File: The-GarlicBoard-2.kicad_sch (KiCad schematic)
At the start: 314 parts, among them J1 TYPE-C-31-M12_13, J2 PAD_SQUARE_1MM, J3 PAD_SQUARE_1MM, J4 PAD_SQUARE_1MM, J5 PAD_SQUARE_1MM, J6 Conn_01x04, K1 SMD-SWITCH-TACTILE-SPST-NO_4P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, Q1 MUN5311DW1T1G, Q2 MUN5311DW1T1G, SW1 RotaryEncoder_Switch, SW10 W, SW11 S, SW12 X, SW13 L_CMD, SW14 E, SW15 D, SW16 C, SW17 R, SW18 F, SW19 V, SW2 ESC, SW20 FN_1, SW21 T, SW22 G, SW23 B, SW24 Y, SW25 H, SW26 N, SW27 SPACE, SW28 U, SW29 J, SW3 TAB, SW30 M, SW31 I, SW32 K, SW33 COMMA, SW34 R_CMD, SW35 O, SW36 L, SW37 PERIOD, SW38 P, SW39 SEMI_COLON, SW4 L_SHIFT, SW40 SLASH, SW41 R_ALT, SW42 HYPHEN, SW43 APOSTROPHE, SW44 R_SHIFT, SW45 R_CTRL, SW46 EQUALS, SW47 RETURN, SW48 FN_2, SW49 BCK_SPC, SW5 L_CTRL, SW50 7, SW51 4, SW52 1, SW53 0, SW54 8, SW55 5, SW56 2, SW57 00, SW58 9, SW59 6, SW6 Q, SW60 3, SW61 NUM_PER, SW62 MINUS, SW63 PLUS, SW64 ENTER, SW65 PAD_LOCK, SW7 A, SW8 Z, SW9 L_ALT, U1 STM32F411CEU6, U2 SRV05-4, U3 SN74LV1T34DCKR, U4 AAP2967-33VIR1, U5 MB85RS64PNF-G-JNERE1, U6 SN74LV1T34DCKR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

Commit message: Conversion from STM32 to RP2040
Removed STM32 MCU and replace with RP2040. Full rewire of board.
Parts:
- removed C1, C35, C36, C38, C42: cap_100nF_16v_0402, Bonsai_C4:C_0402_1005Metric, symbol Bonsai_C4:cap_100nF_16v_0402
- removed C10: cap_10uF_10v_0402, Bonsai_C4:C_0402_1005Metric, symbol Bonsai_C4:cap_10uF_10v_0402
- removed C18, C23: cap_1uF_10v_0402, Bonsai_C4:C_0402_1005Metric, symbol Bonsai_C4:cap_1uF_10v_0402
- removed C31, C43: cap_4.7uF_10v_0402, Bonsai_C4:C_0402_1005Metric, symbol Bonsai_C4:cap_4.7uF_10v_0402
- removed C37: cap_20pF_50v_0402, Bonsai_C4:C_0402_1005Metric, symbol Bonsai_C4:cap_20pF_50v_0402
- removed C48: cap_20pF_50v_0402, Capacitor_SMD:C_0402_1005Metric, symbol Bonsai_C4:cap_20pF_50v_0402
- removed C49, C50: cap_100nF_16v_0402, Capacitor_SMD:C_0402_1005Metric, symbol Bonsai_C4:cap_100nF_16v_0402
- removed D1: SMD-LED-WHITE_0402_, Bonsai_C4:LED_0402, symbol Bonsai_C4:SMD-LED-WHITE_0402_
- removed D2: 1N4148WT, Diode_SMD:D_SOD-523, symbol Diode:1N4148WT
- removed D29: D, Diode_SMD:D_0402_1005Metric, symbol Device:D
- removed D3: SMF5.0A, Bonsai_C4:D_SOD-123FL, symbol Bonsai_C4:SMF5.0A
- removed D4, D5: PMEG2010AEB, Diode_SMD:D_SOD-523, symbol Bonsai_C4:PMEG2010AEB
- removed F1: SMD-PPTC-500MA_0805_, Bonsai_C4:F0805, symbol Bonsai_C4:SMD-PPTC-500MA_0805_
- removed FB1: fb_0402_26ohm, Bonsai_C4:R_0402_1005Metric, symbol Bonsai_C4:fb_0402_26ohm
- removed J1: TYPE-C-31-M12_13, Bonsai_C4:TYPE-C-31-M-12, symbol Bonsai_C4:TYPE-C-31-M12_13
- removed J2: PAD_SQUARE_1MM, Bonsai_C4:PAD_SQUARE_1MM, symbol Bonsai_C4:PAD_SQUARE_1MM
- removed K1: SMD-SWITCH-TACTILE-SPST-NO_4P-2.7MMx3.0MM_, Bonsai_C4:SW4-SMD-2.7X3.0X1.4MM, symbol Bonsai_C4:SMD-SWITCH-TACTILE-SPST-NO_4P-2.7MMx3.0MM_
- removed Q1, Q2: MUN5311DW1T1G, Bonsai_C4:SOT-363_SC-70-6_SC-88, symbol Bonsai_C4:MUN5311DW1T1G
- removed R1: r_470_0402_1p, Bonsai_C4:R_0402_1005Metric, symbol Bonsai_C4:r_470_0402_1p
- removed R11, R6: r_100k_0402_1p, Resistor_SMD:R_0402_1005Metric, symbol Bonsai_C4:r_100k_0402_1p
- removed R2, R3: 5.1k, Keebio-Parts:R_0402, symbol Device:R_Small
- removed R4, R5: r_75_0402_1p, Resistor_SMD:R_0402_1005Metric, symbol Bonsai_C4:r_75_0402_1p
- removed R8, R9: 4.7k, Resistor_SMD:R_0402_1005Metric, symbol Device:R
- removed U1: STM32F411CEU6, Bonsai_C4:QFN-48-1EP_7x7mm_P0.5mm_EP5.6x5.6mm_ThermalVias, symbol Bonsai_C4:STM32F411CEU6
- removed U2: SRV05-4, marbastlib-various:SOT-23-6-routable, symbol Bonsai_C4:SRV05-4
- removed U3: SN74LV1T34DCKR, Bonsai_C4:SOT-353_SC-70-5, symbol Bonsai_C4:SN74LV1T34DCKR
- removed U4: AAP2967-33VIR1, Bonsai_C4:SOT-23-5, symbol Bonsai_C4:AAP2967-33VIR1
- removed U5: MB85RS64PNF-G-JNERE1, Bonsai_C4:SOP-8_3.9x4.9mm_P1.27mm, symbol Bonsai_C4:MB85RS64PNF-G-JNERE1
- removed U7: W25Q128JVSIQ, Bonsai_C4:SOIC-8_5.23x5.23mm_P1.27mm, symbol Bonsai_C4:W25Q128JVSIQ
- removed Y1: SMD-CRYSTAL-8MHZ-20PF-10PPM_2P-5.0X3.2MM_, Bonsai_C4:X2-SMD-5.0X3.2X1.3MM, symbol Bonsai_C4:SMD-CRYSTAL-8MHZ-20PF-10PPM_2P-5.0X3.2MM_
- added C1, C10, C18, C23, C31, C35, C36, C37, C38, C42, C43, C48, C49, C50: 0.1uF, Capacitor_SMD:C_0402_1005Metric, symbol Device:C
- added C79: 27p, Capacitor_SMD:C_0402_1005Metric, symbol Device:C
- added C80: 100n, Capacitor_SMD:C_0402_1005Metric, symbol Device:C
- added D24: D, Diode_SMD:D_0402_1005Metric, symbol Device:D
- added D66: SMF9.0CA, acheron_Components:D_SOD-123_Bidirectional, symbol Device:D_TVS
- added F1: ASMD1206-150, Fuse:Fuse_1206_3216Metric, symbol Device:Polyfuse
- added J1: TYPE-C-31-M12_13, Bonsai_C4:TYPE-C-31-M-12, symbol Unified-Daughterboard-rescue:TYPE-C-31-M12_13-acheronSymbols
- added J6: PAD_SQUARE_1MM, Bonsai_C4:PAD_SQUARE_1MM, symbol Bonsai_C4:PAD_SQUARE_1MM
- added L1: 60R@100MHz, Inductor_SMD:L_1206_3216Metric, symbol Unified-Daughterboard-rescue:L_Core_Ferrite-Device
- added R1, R2: 5.1k, Capacitor_SMD:C_0402_1005Metric, symbol Device:R
- added R11, R5: 1k, Capacitor_SMD:C_0402_1005Metric, symbol Device:R
- added R12, R6: DNF, Capacitor_SMD:C_0402_1005Metric, symbol Device:R
- added R13: 100k, Capacitor_SMD:C_0402_1005Metric, symbol Device:R
- added R3, R4: 27.4, Capacitor_SMD:C_0402_1005Metric, symbol Device:R
- added SW66, SW67: SW_Push, Button_Switch_SMD:SW_SPST_B3U-1000P, symbol Switch:SW_Push
- added U1: RP2040, Package_DFN_QFN:QFN-56-1EP_7x7mm_P0.4mm_EP3.2x3.2mm, symbol MCU_RaspberryPi:RP2040
- added U2: W25Q128JVS, Package_SO:SOIC-8_5.23x5.23mm_P1.27mm, symbol Memory_Flash:W25Q128JVS
- added U3: TPD4E05U06DQAR, acheron_Components:USON-10_2.5x1.0mm_P0.5mm, symbol Unified-Daughterboard-rescue:TPD4E05U06DQAR-acheronSymbols
- added U4: NCP1117-3.3_SOT223, Package_TO_SOT_SMD:SOT-223-3_TabPin2, symbol Regulator_Linear:NCP1117-3.3_SOT223
- added Y1: 12MHz, Crystal:Crystal_SMD_3225-4Pin_3.2x2.5mm, symbol Device:Crystal_GND24_Small
- C65, C66: value 0.1uF -> 10u; footprint Capacitor_SMD:C_0402_1005Metric -> Capacitor_SMD:C_0805_2012Metric
- C67, C68, C70, C72, C73, C74, C75, C76, C77: value 0.1uF -> 100n
- C69, C71: value 0.1uF -> 1u
- C78: value 0.1uF -> 27p
- LED1, LED10, LED11, LED12, LED13, LED14, LED15, LED16, LED17, LED18, LED19, LED2, LED20, LED21, LED22, LED23, LED24, LED25, LED26, LED27, LED28, LED29, LED3, LED30, LED31, LED32, LED33, LED34, LED35, LED36, LED37, LED38, LED39, LED4, LED40, LED41, LED42, LED43, LED44, LED45, LED46, LED47, LED48, LED49, LED5, LED50, LED51, LED52, LED53, LED54, LED55, LED56, LED57, LED58, LED59, LED6, LED60, LED61, LED62, LED63, LED64, LED7, LED8, LED9: value SK6812 -> YS-SK6812MINI-E
- R10: value 4.7k -> 1k; footprint Resistor_SMD:R_0402_1005Metric -> Capacitor_SMD:C_0402_1005Metric
- R7: value 4.7k -> DNF; footprint Resistor_SMD:R_0402_1005Metric -> Capacitor_SMD:C_0402_1005Metric
- U5: renamed from U6; footprint Bonsai_C4:SOT-353_SC-70-5 -> Package_TO_SOT_SMD:SOT-353_SC-70-5
- renumbered D6 to D1, D15 to D10, D16 to D11, D17 to D12, D18 to D13, D19 to D14, D20 to D15, D21 to D16, D22 to D17, D23 to D18, D24 to D19, D7 to D2, D25 to D20, D26 to D21, D27 to D22, D28 to D23, D30 to D25, D31 to D26, D32 to D27, D33 to D28, D34 to D29, D8 to D3, D35 to D30, D36 to D31, D37 to D32, D38 to D33, D39 to D34, D40 to D35, D41 to D36, D42 to D37, D43 to D38, D44 to D39, D9 to D4, D45 to D40, D46 to D41, D47 to D42, D48 to D43, D49 to D44, D50 to D45, D51 to D46, D52 to D47, D53 to D48, D55 to D49, D10 to D5, D56 to D50, D57 to D51, D58 to D52, D59 to D53, D60 to D54, D61 to D55, D62 to D56, D63 to D57, D64 to D58, D65 to D59, D11 to D6, D66 to D60, D67 to D61, D68 to D62, D69 to D63, D70 to D64, D54 to D65, D12 to D7, D13 to D8, D14 to D9, H4 to H2, H2 to H3, H5 to H4, H3 to H5, J6 to J2, SW2 to SW1, SW11 to SW10, SW12 to SW11, SW13 to SW12, SW14 to SW13, SW15 to SW14, SW16 to SW15, SW17 to SW16, SW18 to SW17, SW19 to SW18, SW20 to SW19, SW3 to SW2, SW21 to SW20, SW22 to SW21, SW23 to SW22, SW24 to SW23, SW25 to SW24, SW26 to SW25, SW27 to SW26, SW28 to SW27, SW29 to SW28, SW30 to SW29, SW4 to SW3, SW31 to SW30, SW32 to SW31, SW33 to SW32, SW34 to SW33, SW35 to SW34, SW36 to SW35, SW37 to SW36, SW38 to SW37, SW39 to SW38, SW40 to SW39, SW5 to SW4, SW41 to SW40, SW42 to SW41, SW43 to SW42, SW44 to SW43, SW45 to SW44, SW46 to SW45, SW47 to SW46, SW48 to SW47, SW49 to SW48, SW50 to SW49, SW6 to SW5, SW51 to SW50, SW52 to SW51, SW53 to SW52, SW54 to SW53, SW55 to SW54, SW56 to SW55, SW57 to SW56, SW58 to SW57, SW59 to SW58, SW60 to SW59, SW7 to SW6, SW61 to SW60, SW62 to SW61, SW63 to SW62, SW64 to SW63, SW65 to SW64, SW1 to SW65, SW8 to SW7, SW9 to SW8, SW10 to SW9
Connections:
- net +3V3: now also C66.1, C70.1, C71.1, C72.1, C73.1, C74.1, C75.1, C76.1, C77.1, R7.2, C80.1, R12.2, R13.2, R5.2, R6.2, U1.1 (IOVDD), U1.10 (IOVDD), U1.22 (IOVDD), U1.33 (IOVDD), U1.42 (IOVDD), U1.43 (ADC_AVDD), U1.44 (VREG_IN), U1.48 (USB_VDD), U1.49 (IOVDD), U2.8 (VCC), U4.2 (VO); no longer R10.1, R7.1
- net +5V: now also C1.1, C10.1, C18.1, C23.1, C31.1, C35.1, C36.1, C37.1, C38.1, C42.1, C43.1, C48.1, C49.1, C50.1, D66.2 (A2), F1.2, U4.3 (VI); no longer C66.1, C67.1, C68.1, C69.1, C70.1, C71.1, C72.1, C73.1, C74.1, C75.1, C76.1, C77.1, C78.1
- net COL0: now also U1.27 (GPIO16)
- net COL1: now also U1.28 (GPIO17)
- net COL2: now also U1.29 (GPIO18)
- net COL3: now also U1.30 (GPIO19)
- net COL4: now also U1.31 (GPIO20)
- net COL5: now also U1.32 (GPIO21)
- net COL6: now also U1.34 (GPIO22)
- net COL7: now also U1.6 (GPIO4)
- net COL8: now also U1.7 (GPIO5)
- net ENC_A: now also U1.40 (GPIO28_ADC2); no longer R10.2
- net ENC_B: now also U1.41 (GPIO29_ADC3)
- net GND: now also C78.1, C1.2, C10.2, C18.2, C23.2, C31.2, C35.2, C36.2, C37.2, C38.2, C42.2, C43.2, C48.2, C49.2, C50.2, C79.1, C80.2, L1.1, SW66.1, SW67.1, U1.19 (TESTEN), U1.57 (GND), U2.4 (GND), U4.1 (GND), Y1.2, Y1.4; no longer C78.2
- net ROW0: now also U1.2 (GPIO0)
- net ROW1: now also D24.1 (K), U1.4 (GPIO2)
- net ROW2: now also U1.8 (GPIO6)
- net ROW3: now also U1.13 (GPIO10)
- net ROW4: now also U1.3 (GPIO1)
- net ROW5: now also U1.5 (GPIO3)
- net ROW6: now also U1.9 (GPIO7)
- net ROW7: now also U1.14 (GPIO11)
- net SCL: now also R7.1, U1.18 (GPIO15)
- net SDA: now also R6.1, U1.17 (GPIO14); no longer R7.2
- net SWCLK: now also U1.24 (SWCLK)
- net SWDIO: now also U1.25 (SWD)
- net VBUS: now also F1.1, J1.A4 (VBUS), J1.B4 (VBUS)
- net at LED37.4 (DIN): now also LED36.2 (DOUT); no longer LED33.2 (DOUT)
- net at LED33.4 (DIN): now also LED32.2 (DOUT); no longer LED34.2 (DOUT)
- net at LED53.2 (DOUT): now also LED54.4 (DIN); no longer LED57.4 (DIN)
- net at LED53.4 (DIN): now also LED52.2 (DOUT); no longer LED54.2 (DOUT)
- net at LED41.2 (DOUT): now also LED42.4 (DIN); no longer LED44.4 (DIN)
- net at LED41.4 (DIN): now also LED40.2 (DOUT); no longer LED42.2 (DOUT)
- net at LED13.2 (DOUT): now also LED14.4 (DIN); no longer LED16.4 (DIN)
- net at LED13.4 (DIN): now also LED12.2 (DOUT); no longer LED14.2 (DOUT)
- net at LED56.4 (DIN): now also LED55.2 (DOUT); no longer LED52.2 (DOUT)
- net at LED15.2 (DOUT): now also LED16.4 (DIN); no longer LED14.4 (DIN)
- net at LED30.4 (DIN): now also LED29.2 (DOUT); no longer LED27.2 (DOUT)
- net at LED60.2 (DOUT): now also LED61.4 (DIN); no longer LED64.4 (DIN)
- net at LED34.4 (DIN): now also LED33.2 (DOUT); no longer LED35.2 (DOUT)
- net at LED49.4 (DIN): now also LED48.2 (DOUT); no longer LED47.2 (DOUT)
- net at LED47.4 (DIN): now also LED46.2 (DOUT); no longer LED48.2 (DOUT)
- net at LED20.4 (DIN): now also LED19.2 (DOUT); no longer LED21.2 (DOUT)
- net at LED22.2 (DOUT): now also LED23.4 (DIN); no longer LED21.4 (DIN)
- net at LED35.4 (DIN): now also LED34.2 (DOUT); no longer LED36.2 (DOUT)
- net at LED36.4 (DIN): now also LED35.2 (DOUT); no longer LED32.2 (DOUT)
- net at LED48.4 (DIN): now also LED47.2 (DOUT); no longer LED46.2 (DOUT)
- net at LED20.2 (DOUT): now also LED21.4 (DIN); no longer LED23.4 (DIN)
- net at SW24.1: now also D24.2 (A)
- net at LED43.2 (DOUT): now also LED44.4 (DIN); no longer LED42.4 (DIN)
- net at LED43.4 (DIN): now also LED42.2 (DOUT); no longer LED40.2 (DOUT)
- net at LED5.2 (DOUT): now also LED6.4 (DIN); no longer LED9.4 (DIN)
- net at LED5.4 (DIN): now also LED4.2 (DOUT); no longer LED6.2 (DOUT)
- net at LED15.4 (DIN): now also LED14.2 (DOUT); no longer LED12.2 (DOUT)
- net at LED7.4 (DIN): now also LED6.2 (DOUT); no longer LED8.2 (DOUT)
- net at LED8.4 (DIN): now also LED7.2 (DOUT); no longer LED4.2 (DOUT)
- net at LED29.4 (DIN): now also LED28.2 (DOUT); no longer LED26.2 (DOUT)
- net at LED27.4 (DIN): now also LED26.2 (DOUT); no longer LED28.2 (DOUT)
- net at LED22.4 (DIN): now also LED21.2 (DOUT); no longer LED19.2 (DOUT)
- net at LED28.4 (DIN): now also LED27.2 (DOUT); no longer LED29.2 (DOUT)
- net at LED55.4 (DIN): now also LED54.2 (DOUT); no longer LED56.2 (DOUT)
- net at LED63.4 (DIN): now also LED62.2 (DOUT); no longer LED64.2 (DOUT)
- net at LED61.2 (DOUT): now also LED62.4 (DIN)
- net at LED63.2 (DOUT): now also LED64.4 (DIN); no longer LED62.4 (DIN)
- net A10 renamed RGB
- net RGB: now also R13.1, U1.39 (GPIO27_ADC1)
- net A10_5V renamed RGB_5V
- net B2: no longer names the net of J3.1
- net B2: now also U1.35 (GPIO23)
- net BOOT0: no longer names the net of J5.1
- net BOOT0: now also U1.37 (GPIO25)
- net NRST: no longer names the net of J4.1
- net NRST: now also U1.36 (GPIO24)
- new net: R4.2, U1.46 (USB_DM)
- new net: J6.1, U1.38 (GPIO26_ADC0)
- new net: C79.2, R10.1, Y1.1
- new net: R3.2, U1.47 (USB_DP)
- new net: J1.B5 (CC2), R2.2
- new net: LED8.2 (DOUT), LED9.4 (DIN)
- new net: LED56.2 (DOUT), LED57.4 (DIN)
- new net: J1.A5 (CC1), R1.1
- new net +1V1: C67.1, C68.1, C69.1, U1.23 (DVDD), U1.45 (VREG_VOUT), U1.50 (DVDD)
- new net DA+: J1.A6 (D+), J1.B6 (D+), R3.1, U3.1 (IO1), U3.10 (NC), U3.4 (D2+), U3.7 (NC)
- new net DA-: J1.A7 (D-), J1.B7 (D-), R4.1, U3.2 (IO2), U3.5 (D2-), U3.6 (NC), U3.9 (NC)
- new net GNDPWR: D66.1 (A1), J1.A1 (GND), J1.B1 (GND), J1.S (SHIELD), L1.2, R1.2, R2.1, U3.3 (GND), U3.8 (GND)
- new net QSPI_SCLK: U1.52 (QSPI_SCLK), U2.6 (CLK)
- new net QSPI_SD0: U1.53 (QSPI_SD0), U2.5 (DI(IO0))
- new net QSPI_SD1: U1.55 (QSPI_SD1), U2.2 (DO(IO1))
- new net QSPI_SD2: U1.54 (QSPI_SD2), U2.3 (IO2)
- new net QSPI_SD3: U1.51 (QSPI_SD3), U2.7 (IO3)
- new net QSPI_SS: R11.2, R12.1, U1.56 (QSPI_SS), U2.1 (~{CS})
- new net RESET: R5.1, SW66.2, U1.26 (RUN)
- new net XIN: C78.2, U1.20 (XIN), Y1.3
- new net XOUT: R10.2, U1.21 (XOUT)
- new net ~{USB_BOOT}: R11.1, SW67.2
- no-connect marks 11 -> 7
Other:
- note added: "5V to drive SK6812-mini-e"
- note added: "CLOCK"
- note added: "MCU TO LED STRAND"
- note added: "RESET"
- note added: "STORAGE"
- note added: "The GarlicBoard stiligFox"
- note added: "USB AND ESD"
- note removed: "+"
- note removed: ","
- note removed: "."
- note removed: "/"
- note removed: "0"
- note removed: "00"
- note removed: "1"
- note removed: "1mm square pads on back"
- note removed: "2"
- note removed: "3"
- note removed: "4"
- note removed: "5"
- note removed: "5V to drive WS2812"
- note removed: "6"
- note removed: "7"
- note removed: "8"
- note removed: "9"
- note removed: ";"
- note removed: "="
- note removed: "A"
- note removed: "A10 TO RGB LED STRAND"
- note removed: "B"
- note removed: "BCK SPC"
- note removed: "BOOT"
- note removed: "BOOT1"
- note removed: "C"
- note removed: "CRYSTAL"
- note removed: "D"
- note removed: "E"
- note removed: "EMERGENCY PADS"
- note removed: "ENTER"
- note removed: "ESC"
- note removed: "F"
- note removed: "FN_1"
- note removed: "FN_2"
- note removed: "FRAM AND FLASH"
- note removed: "G"
- note removed: "H"
- note removed: "I"
- note removed: "J"
- note removed: "K"
- note removed: "L"
- note removed: "L_ALT"
- note removed: "L_CMD"
- note removed: "L_CTRL"
- note removed: "L_SHIFT"
- note removed: "M"
- note removed: "N"
- note removed: "O"
- note removed: "P"
- note removed: "PAD LOCK"
- note removed: "PERIOD"
- note removed: "POWER SUPPLY"
- note removed: "Q"
- note removed: "R"
- note removed: "RESET CIRCUIT"
- note removed: "RETURN"
- note removed: "R_ALT"
- note removed: "R_CMD"
- note removed: "R_CTRL"
- note removed: "R_SHIFT"
- note removed: "S"
- note removed: "SPACE"
- note removed: "T"
- note removed: "TAB"
- note removed: "TO RGB STRAND"
- note removed: "The GarlicBoard Thomas Meyer"
- note removed: "U"
- note removed: "USB CONNECTOR AND ESD"
- note removed: "V"
- note removed: "W"
- note removed: "X"
- note removed: "Y"
- note removed: "Z"
- moved on the sheet: D1, D10, D11, D12, D13, D14, D15, D16, D17, D18, D19, D2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

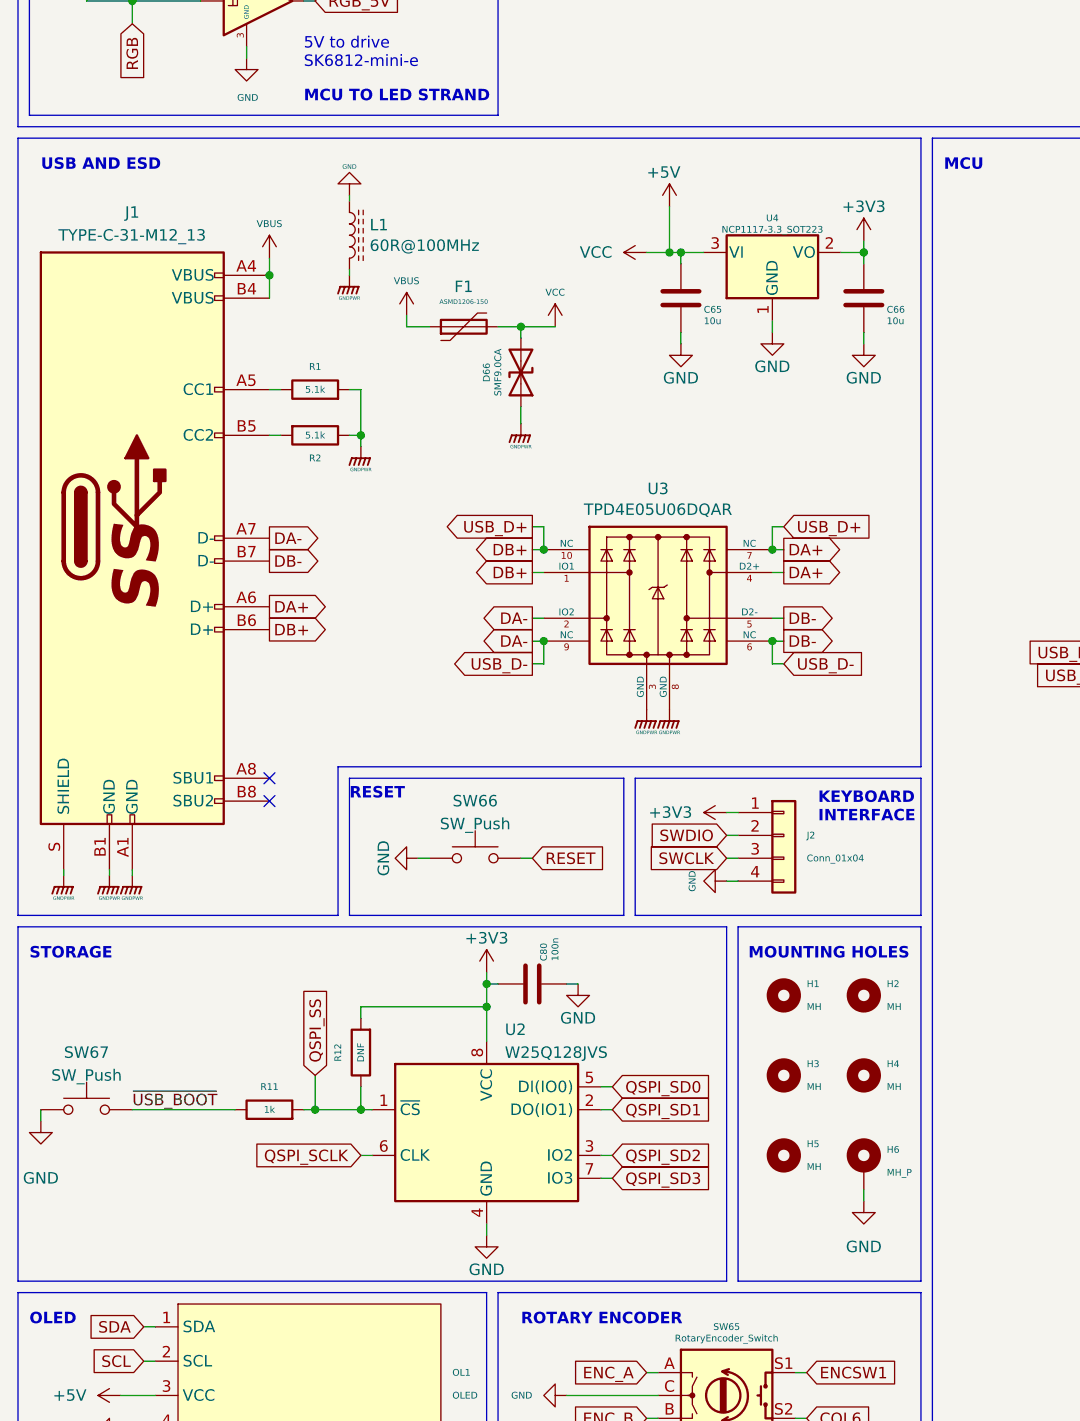
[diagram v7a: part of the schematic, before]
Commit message: Updated USB circuitry
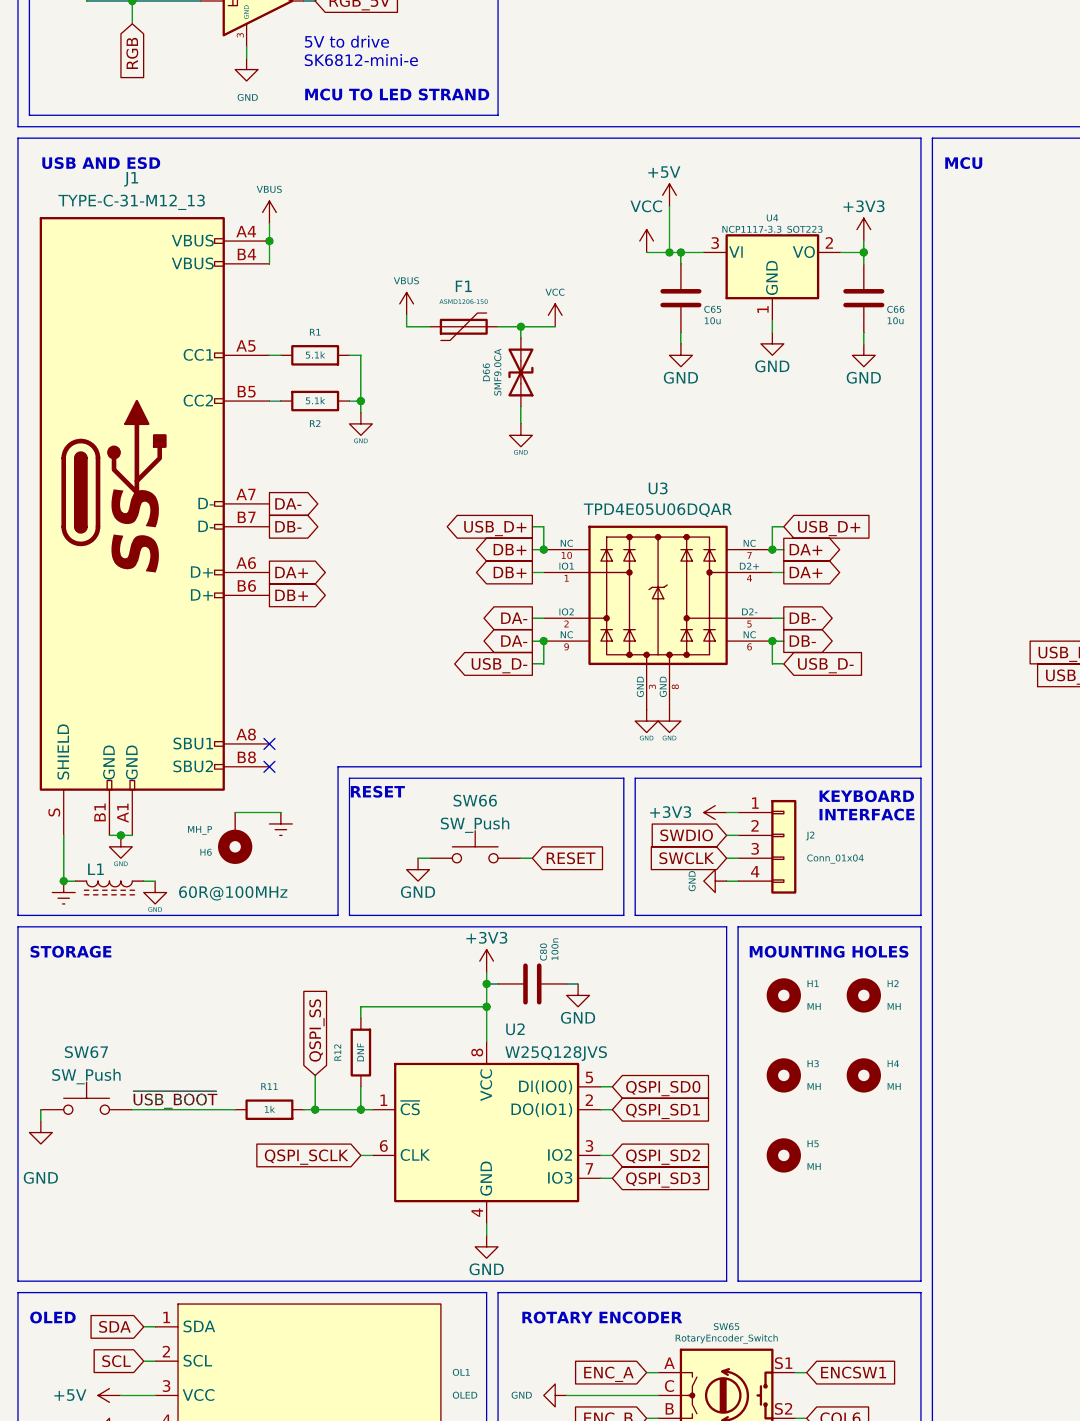
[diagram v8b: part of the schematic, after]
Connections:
- net GND: now also D66.1 (A1), J1.A1 (GND), J1.B1 (GND), R1.2, R2.1, U3.3 (GND), U3.8 (GND); no longer H6.1
- removed net GNDPWR: D66.1 (A1), J1.A1 (GND), J1.B1 (GND), J1.S (SHIELD), L1.2, R1.2, R2.1, U3.3 (GND), U3.8 (GND)
- new net Earth: H6.1, J1.S (SHIELD), L1.2
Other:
- moved on the sheet: J1, L1, R1, R2
